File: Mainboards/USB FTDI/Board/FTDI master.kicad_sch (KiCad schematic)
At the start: 52 parts, among them IC1 NCP1117ST, IC10 FT232RL, IC2 MCP1700T-1802E, IC3 CRE1S0505SC, IC4 IL0512S, IC5 IRF7416, IC7 ADuM142E0BRQZ-RL7, IC8 ADuM142E0BRQZ-RL7, IC9 ADuM142E0BRQZ-RL7, J1 USB_C_Receptacle_USB2.0, X2 AKL18X-04W, X3 IDC-Header_2x05_P2.54mm_Verti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, X4 ALLSERIALMASTERM

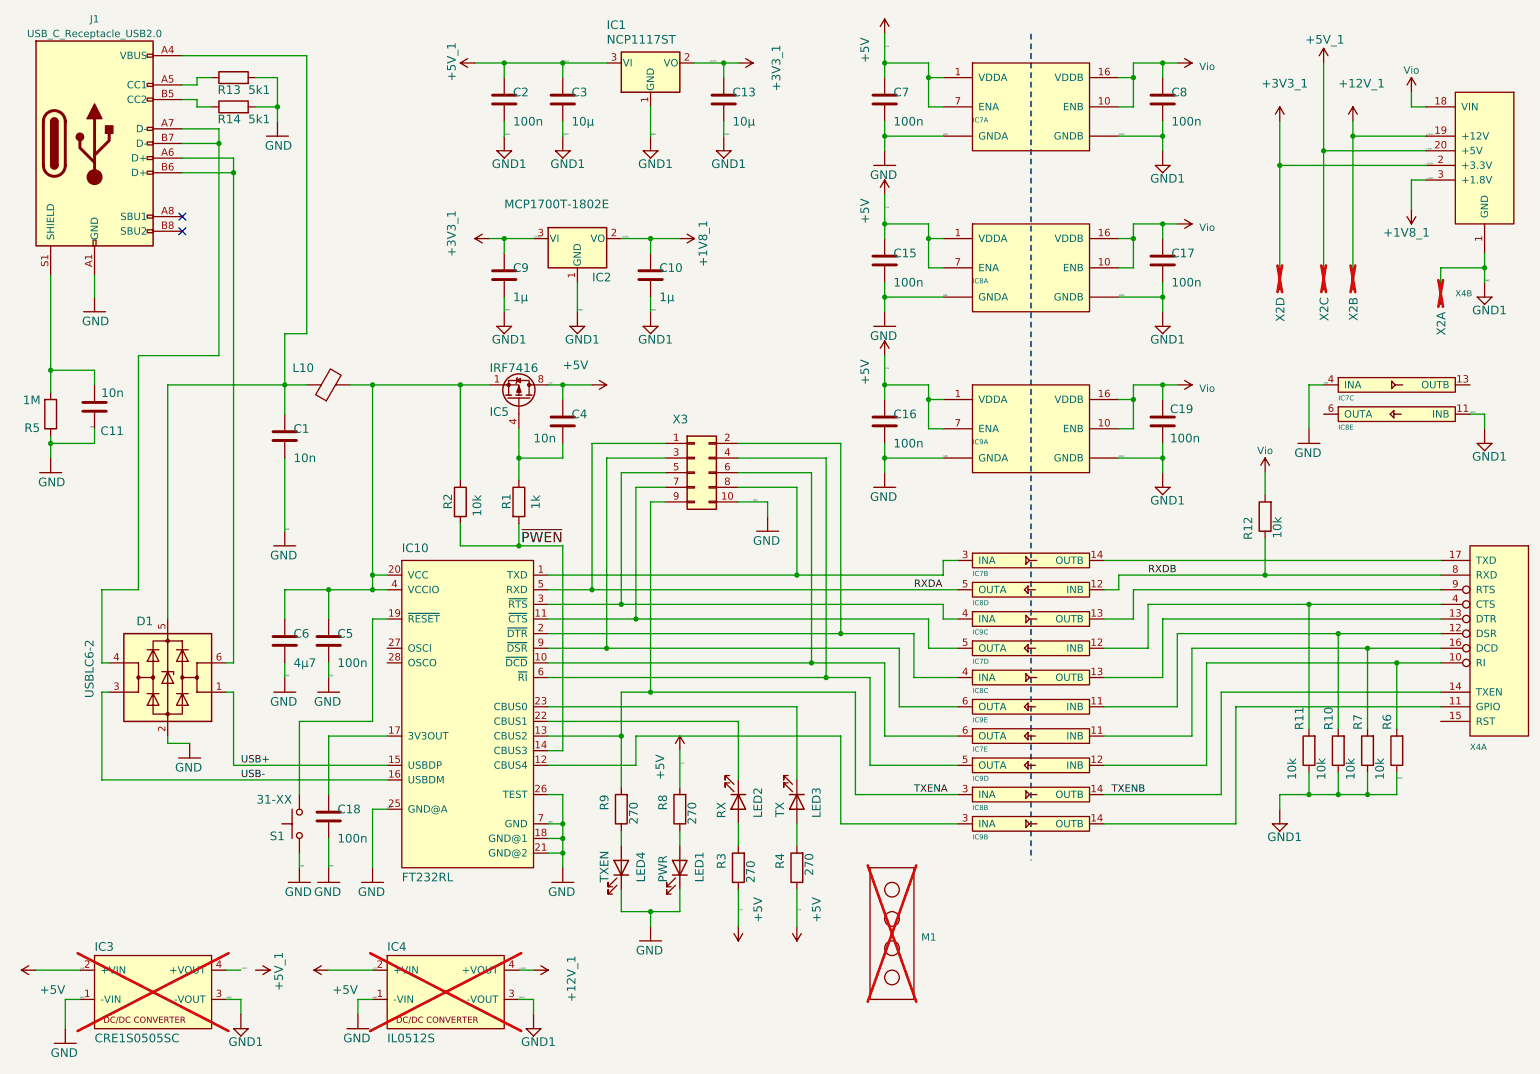
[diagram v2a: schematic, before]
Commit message: Migrate to KiCad 9
Add eBus board
Add various libraries
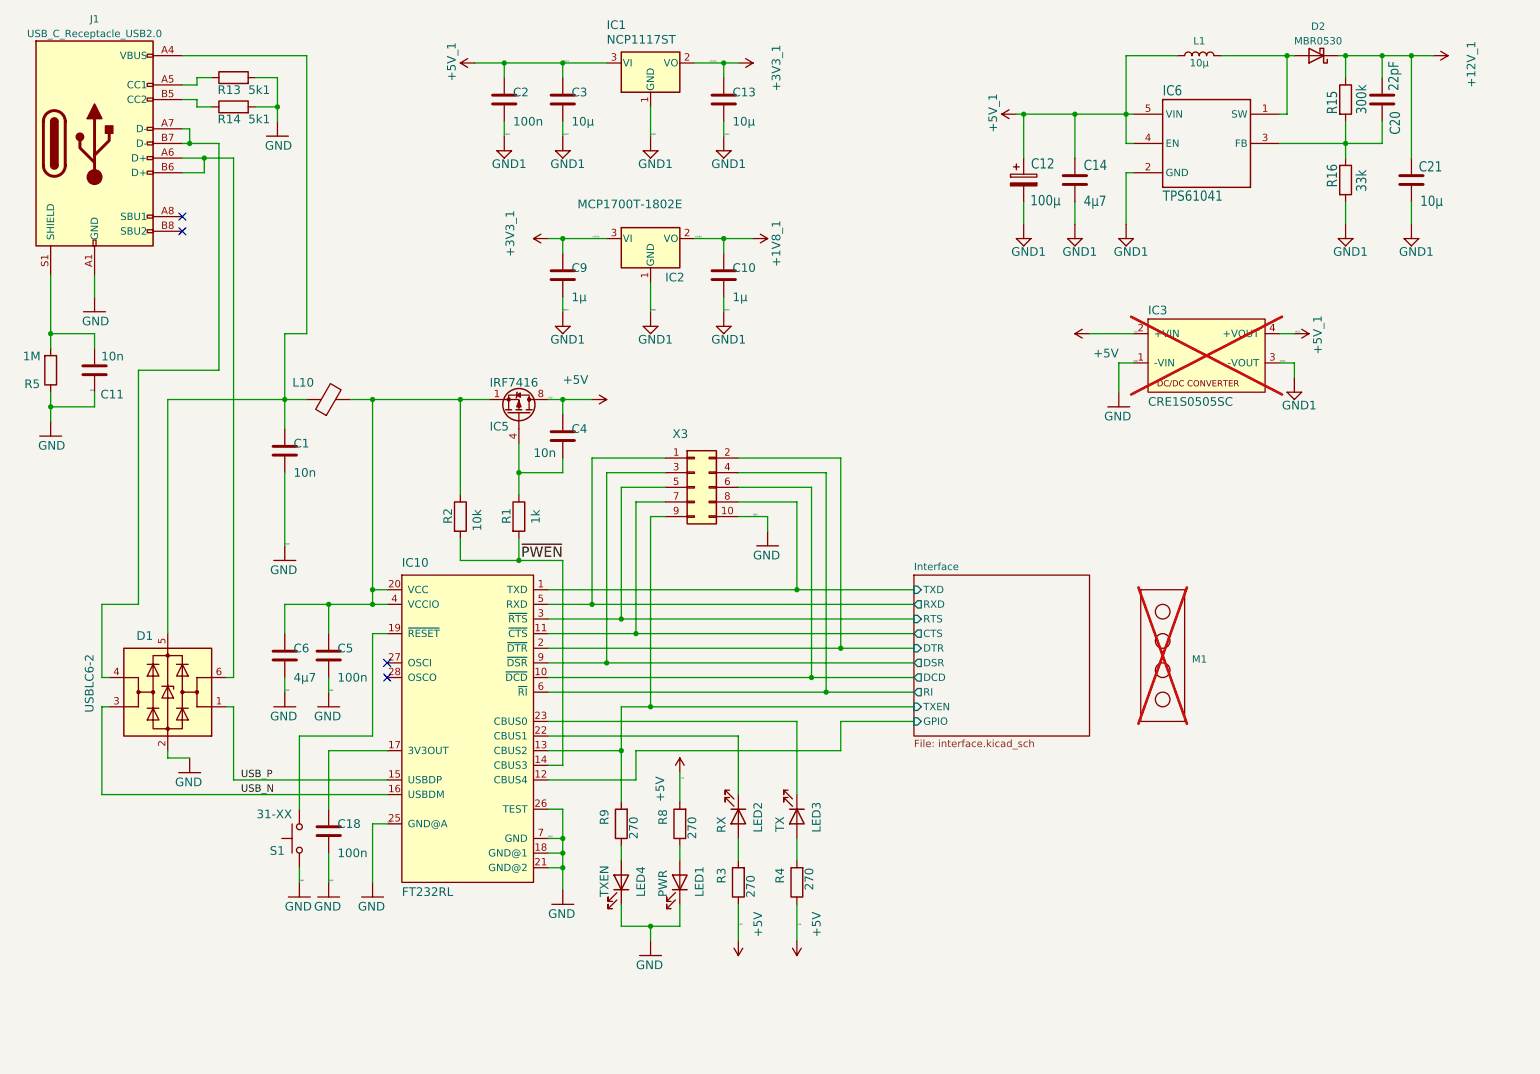
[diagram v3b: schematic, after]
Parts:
- removed C15, C16, C17, C19, C7, C8: 100n, Capacitor_SMD:C_0603_1608Metric, symbol Device:C
- removed IC4: IL0512S, AllSerial:XPPOWER-ILxxxxS, symbol AllSerial:DCDC_Converter
- removed IC7, IC8, IC9: ADuM142E0BRQZ-RL7, Package_SO:QSOP-16_3.9x4.9mm_P0.635mm, symbol AllSerial:ADuM142
- removed R10, R11, R12, R6, R7: 10k, Resistor_SMD:R_0805_2012Metric, symbol Device:R
- removed X2: AKL18X-04W, AllSerial:Metz_PT11304HBBN_182, symbol FTDI_master-eagle-import:AKL18X-04W
- removed X4: ALLSERIALMASTERM, AllSerial:MasterBoard, symbol AllSerial:AllSerial_Connector
- added C12: 100µ, Capacitor_SMD:CP_Elec_5x5.9, symbol Device:C_Polarized
- added C14: 4µ7, Capacitor_SMD:C_0805_2012Metric, symbol Device:C
- added C20: 22pF, Capacitor_SMD:C_0805_2012Metric, symbol Device:C
- added C21: 10µ, Capacitor_SMD:C_0805_2012Metric, symbol Device:C
- added D2: MBR0530, Diode_SMD:D_SOD-123, symbol Device:D_Schottky
- added IC6: TPS61041, Package_TO_SOT_SMD:SOT-23-5_HandSoldering, symbol minirx_v4-eagle-import:TPS61040
- added L1: 10µ, Inductor_SMD:L_1210_3225Metric, symbol Device:L
- added R15: 300k, Resistor_SMD:R_0805_2012Metric, symbol Device:R
- added R16: 33k, Resistor_SMD:R_0805_2012Metric, symbol Device:R
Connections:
- net +12V_1: now also C20.1, C21.1, D2.1 (K), R15.1
- net +5V_1: now also C12.1, C14.1, IC6.4 (EN), IC6.5 (VIN), L1.1
- net GND1: now also C12.2, C14.2, C21.2, IC6.2 (GND), R16.2
- net Interface/CTS: now reaches IC10.11 (~{CTS}), X3.7 (Pin_7)
- net Interface/DCD: now reaches IC10.10 (~{DCD}), X3.6 (Pin_6)
- net Interface/TXD: now reaches IC10.1 (TXD), X3.8 (Pin_8)
- net Interface/GPIO: now reaches IC10.12 (CBUS4)
- net Interface/DTR: now reaches IC10.2 (~{DTR}), X3.2 (Pin_2)
- net Interface/RTS: now reaches IC10.3 (~{RTS}), X3.5 (Pin_5)
- net Interface/RI: now reaches IC10.6 (~{RI}), X3.4 (Pin_4)
- net Interface/DSR: now reaches IC10.9 (~{DSR}), X3.3 (Pin_3)
- net RXDA renamed Interface/RXD
- net TXENA renamed Interface/TXEN
- net USB+ renamed USB_P
- net USB- renamed USB_N
- new net: D2.2 (A), IC6.1 (SW), L1.2
- new net: C20.2, IC6.3 (FB), R15.2, R16.1
- no-connect marks 2 -> 4
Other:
- added sheet Interface (interface.kicad_sch)
- moved on the sheet: C1, C10, C11, C18, C4, C5, C6, C9, D1, IC10, IC2, IC3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

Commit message: Improve libraries
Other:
- moved on the sheet: IC3, M1
